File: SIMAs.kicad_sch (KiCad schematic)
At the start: 4 parts, among them U1 mini_esp32, U2 BQ25628ERYKR, U3 TLV61070ADBV, U4 TLV61048DBVR

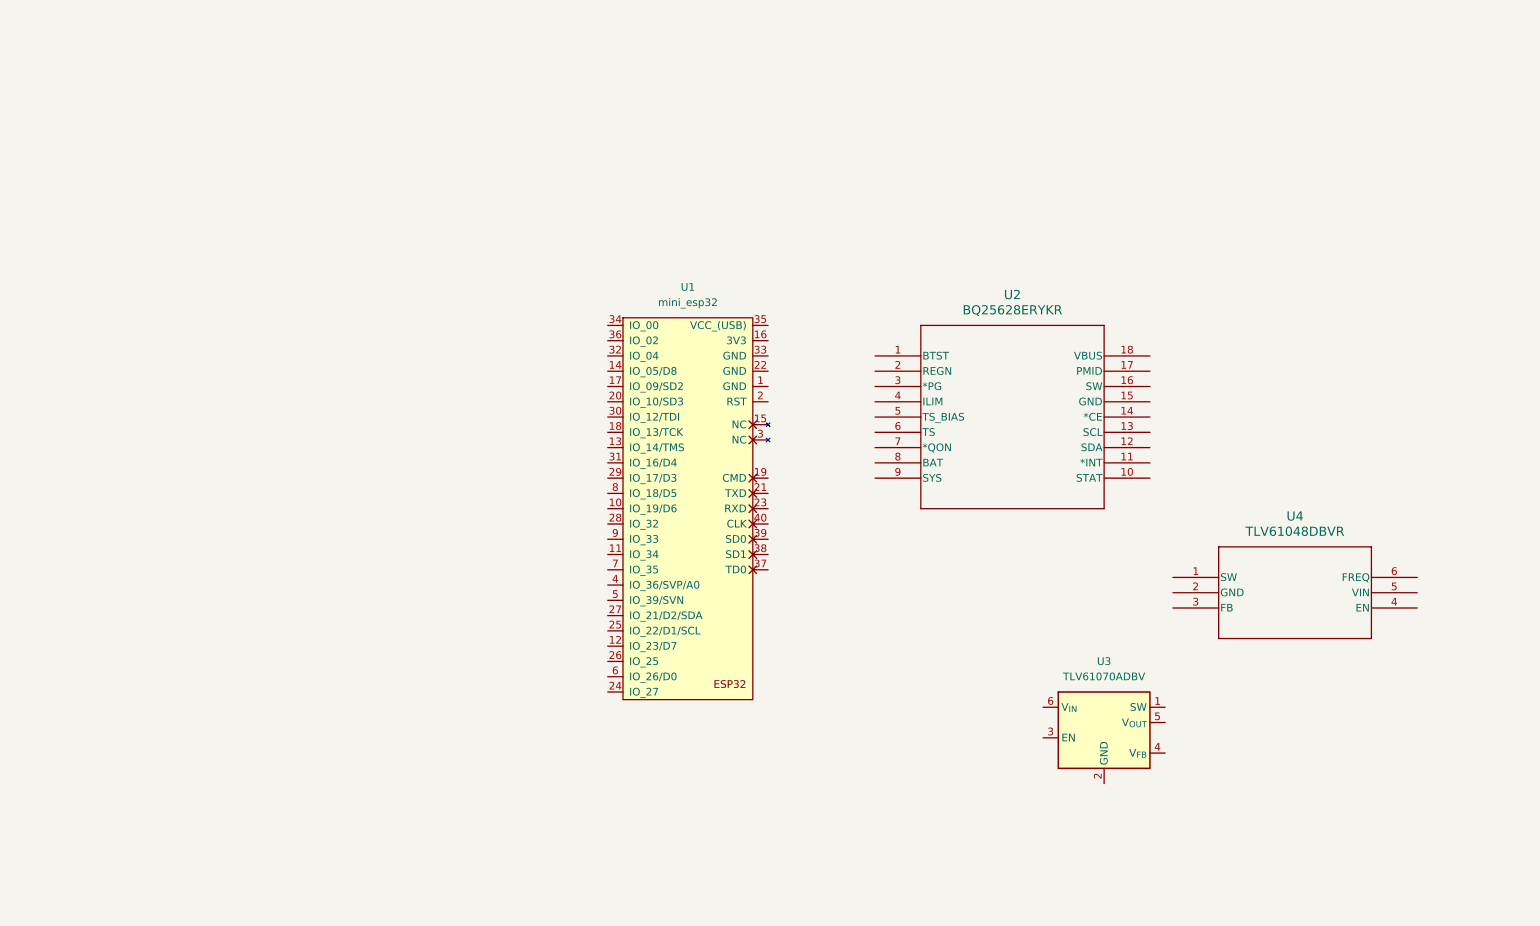
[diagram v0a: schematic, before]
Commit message: Battery charger and 5V boost
Added a herarchical sheet for the poers supply. Done the battery charger and monitor schematic with USB-C charging and the 5 V boost.
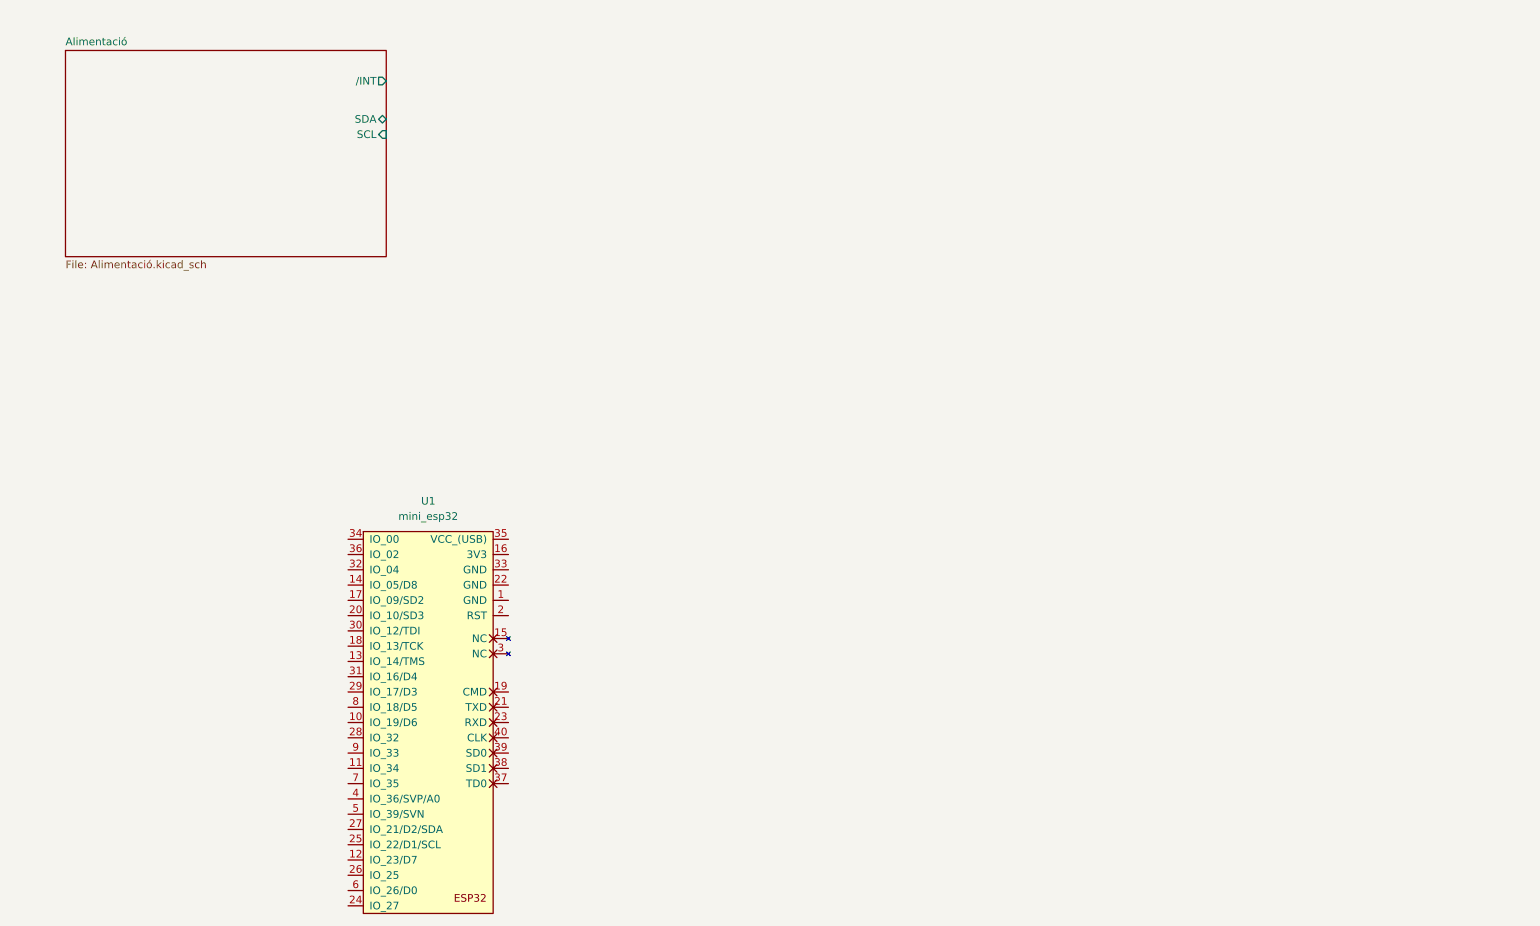
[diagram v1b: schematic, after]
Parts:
- removed U2: BQ25628ERYKR, WQFN-HR18__RYK_TEX, symbol BQ25628E:BQ25628ERYKR
- removed U3: TLV61070ADBV, Package_TO_SOT_SMD:SOT-23-6, symbol Regulator_Switching:TLV61070ADBV
- removed U4: TLV61048DBVR, SOT-23-6_DBV_TEX, symbol TLV61048:TLV61048DBVR
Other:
- added sheet Alimentació (Alimentació.kicad_sch)
- moved on the sheet: U1

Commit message: Canvi
Algu ha canviat, no recordo
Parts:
- added R10, R12, R8: 110, symbol Device:R
- added R11, R13, R9: 2,2 k, symbol Device:R
- added U5, U6, U7: CNY70, OptoDevice:Vishay_CNY70, symbol Sensor_Proximity:CNY70
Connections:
- new net: R10.1, U6.1 (A)
- new net: R12.1, U7.1 (A)
- new net: R8.1, U5.1 (A)
- new net +3.3V: R10.2, R11.2, R12.2, R13.2, R8.2, R9.2
- new net GND: U5.2 (K), U5.4 (E), U6.2 (K), U6.4 (E), U7.2 (K), U7.4 (E)
- new net SENSE_LLUM_1: R9.1, U5.3 (C)
- new net SENSE_LLUM_2: R11.1, R13.1, U6.3 (C), U7.3 (C)
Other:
- added sheet Motors (Motors.kicad_sch)

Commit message: actualitzar ultrima versio pcb/esquematic
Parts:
- added J3, J4, J5: Conn_01x04_Socket, Connector_JST:JST_PH_B4B-PH-K_1x04_P2.00mm_Vertical, symbol Connector:Conn_01x04_Socket
- added J6: Conn_01x03_Socket, Connector_JST:JST_PH_B3B-PH-K_1x03_P2.00mm_Vertical, symbol Connector:Conn_01x03_Socket
- added R28, R29, R30: 110, Resistor_SMD:R_0201_0603Metric, symbol Device:R
- R10, R11, R12, R13, R8, R9: footprint (none) -> Resistor_SMD:R_0201_0603Metric
- U1: footprint (none) -> ESP32_mini:ESP32_mini
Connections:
- net +3.3V: now also J3.1 (Pin_1), J4.1 (Pin_1)
- net Alimentació/SCL: now also U1.25 (IO_22/D1/SCL), R30.1
- net Alimentació/SDA: now also U1.27 (IO_21/D2/SDA), R29.1
- net Alimentació//INT: now also U1.29 (IO_17/D3), R28.1
- net GND: now also U1.22 (GND), J3.4 (Pin_4), J4.4 (Pin_4), J5.4 (Pin_4), J6.3 (Pin_3)
- net ENC3: now reaches U1.11 (IO_34)
- net ENC3: now also J4.2 (Pin_2)
- net nFAULT2: now reaches U1.13 (IO_14/TMS)
- net nFAULT1: now reaches U1.14 (IO_05/D8)
- net at U1.16 (3V3): now also R28.2, R29.2, R30.2
- net IPROPI1: now reaches U1.17 (IO_09/SD2)
- net nSLEEP2: now reaches U1.18 (IO_13/TCK)
- net EN/IN3: now reaches U1.20 (IO_10/SD3)
- net SERVO: now reaches U1.24 (IO_27)
- net SERVO: now also J6.2 (Pin_2)
- net SONS1: now reaches U1.26 (IO_25)
- net SONS1: now also J5.2 (Pin_2)
- net ENC1: now reaches U1.28 (IO_32)
- net ENC1: now also J3.2 (Pin_2)
- net PH/IN4: now reaches U1.30 (IO_12/TDI)
- net IPROPI2: now reaches U1.31 (IO_16/D4)
- net nSLEEP1: now reaches U1.32 (IO_04)
- net EN/IN1: now reaches U1.34 (IO_00)
- net +5V: now reaches U1.35 (VCC_(USB))
- net +5V: now also J5.1 (Pin_1), J6.1 (Pin_1)
- net PH/IN2: now reaches U1.36 (IO_02)
- net SONS2: now reaches U1.6 (IO_26/D0)
- net SONS2: now also J5.3 (Pin_3)
- net ENC4: now reaches U1.7 (IO_35)
- net ENC4: now also J4.3 (Pin_3)
- net ENC2: now reaches U1.9 (IO_33)
- net ENC2: now also J3.3 (Pin_3)
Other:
- moved on the sheet: U1

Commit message: esquematic fet v1
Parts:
- R10, R11, R12, R13, R28, R29, R30, R8, R9: footprint Resistor_SMD:R_0201_0603Metric -> Resistor_SMD:R_0603_1608Metric
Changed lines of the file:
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@@
 			)
 		)
-		(property "Footprint" "Resistor_SMD:R_0201_0603Metric"
+		(property "Footprint" "Resistor_SMD:R_0603_1608Metric"
 			(at 25.908 128.27 90)
 			(effects
@@
 			)
 		)
-		(property "Footprint" "Resistor_SMD:R_0201_0603Metric"
+		(property "Footprint" "Resistor_SMD:R_0603_1608Metric"
 			(at 257.048 33.02 90)
 			(effects
@@
 			)
 		)
-		(property "Footprint" "Resistor_SMD:R_0201_0603Metric"
+		(property "Footprint" "Resistor_SMD:R_0603_1608Metric"
 			(at 185.928 33.02 90)
 			(effects
@@
 			)
 		)
-		(property "Footprint" "Resistor_SMD:R_0201_0603Metric"
+		(property "Footprint" "Resistor_SMD:R_0603_1608Metric"
 			(at 208.788 33.02 90)
 			(effects
@@
 			)
 		)
-		(property "Footprint" "Resistor_SMD:R_0201_0603Metric"
+		(property "Footprint" "Resistor_SMD:R_0603_1608Metric"
 			(at 34.798 128.27 90)
 			(effects
@@
 			)
 		)
-		(property "Footprint" "Resistor_SMD:R_0201_0603Metric"
+		(property "Footprint" "Resistor_SMD:R_0603_1608Metric"
 			(at 43.688 128.27 90)
 			(effects
@@
 			)
 		)
-		(property "Footprint" "Resistor_SMD:R_0201_0603Metric"
+		(property "Footprint" "Resistor_SMD:R_0603_1608Metric"
 			(at 160.528 33.02 90)
 			(effects
@@
 			)
 		)
-		(property "Footprint" "Resistor_SMD:R_0201_0603Metric"
+		(property "Footprint" "Resistor_SMD:R_0603_1608Metric"
 			(at 137.668 33.02 90)
 			(effects
@@
 			)
 		)
-		(property "Footprint" "Resistor_SMD:R_0201_0603Metric"
+		(property "Footprint" "Resistor_SMD:R_0603_1608Metric"
 			(at 234.188 33.02 90)
 			(effects

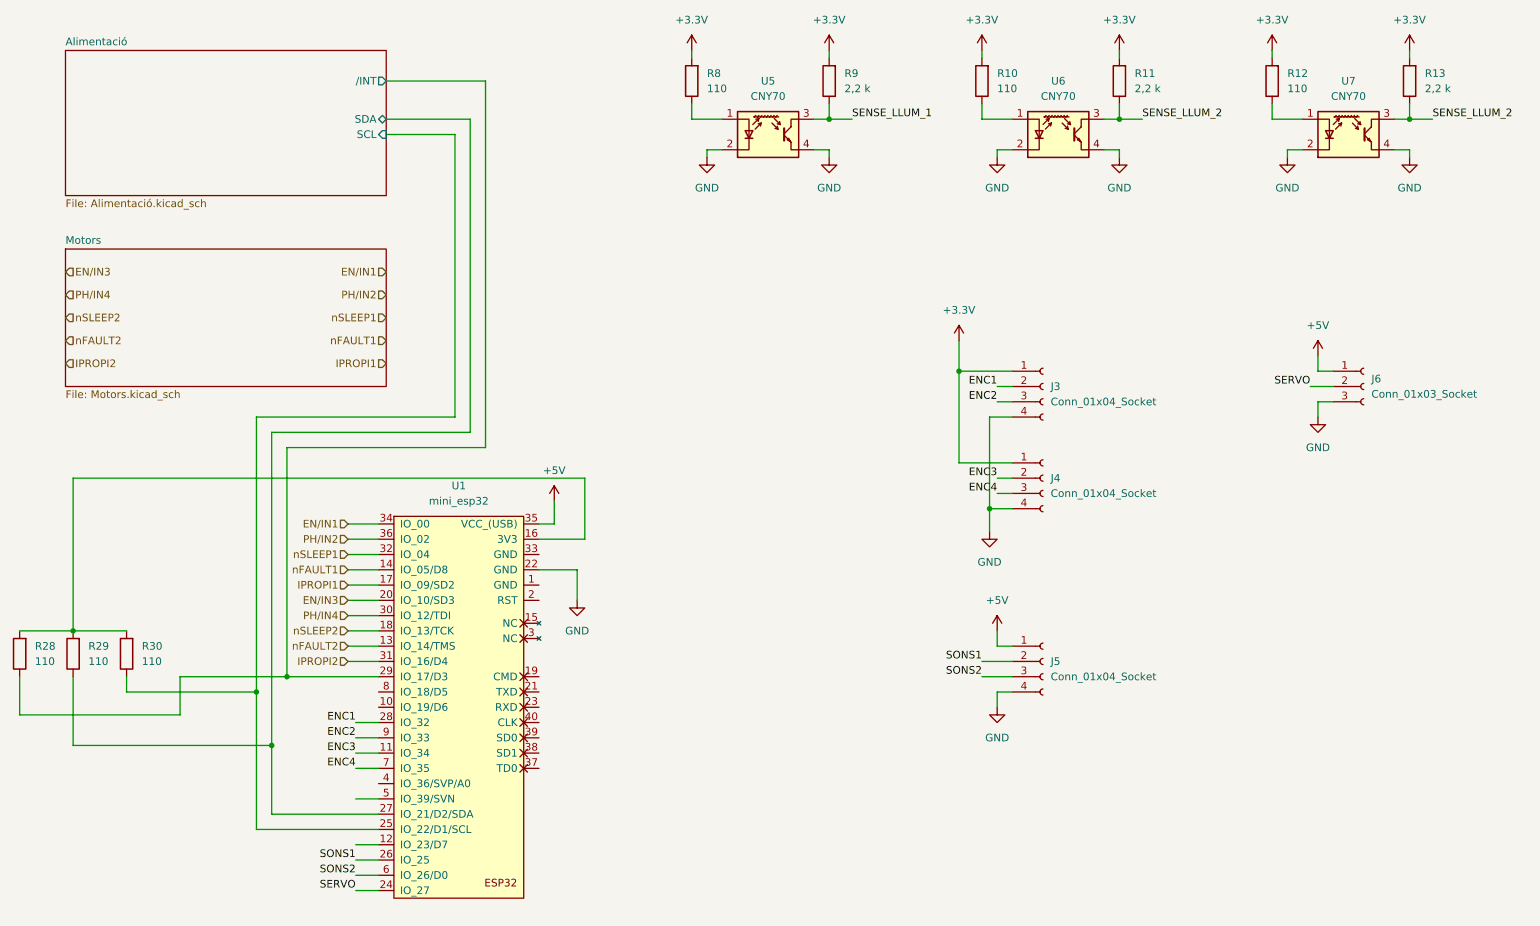
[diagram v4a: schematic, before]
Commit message: Col·locats tots els components
S'han col·locat tots els components a la seva posició a la placa a més d'haver-ne afegit algun més.
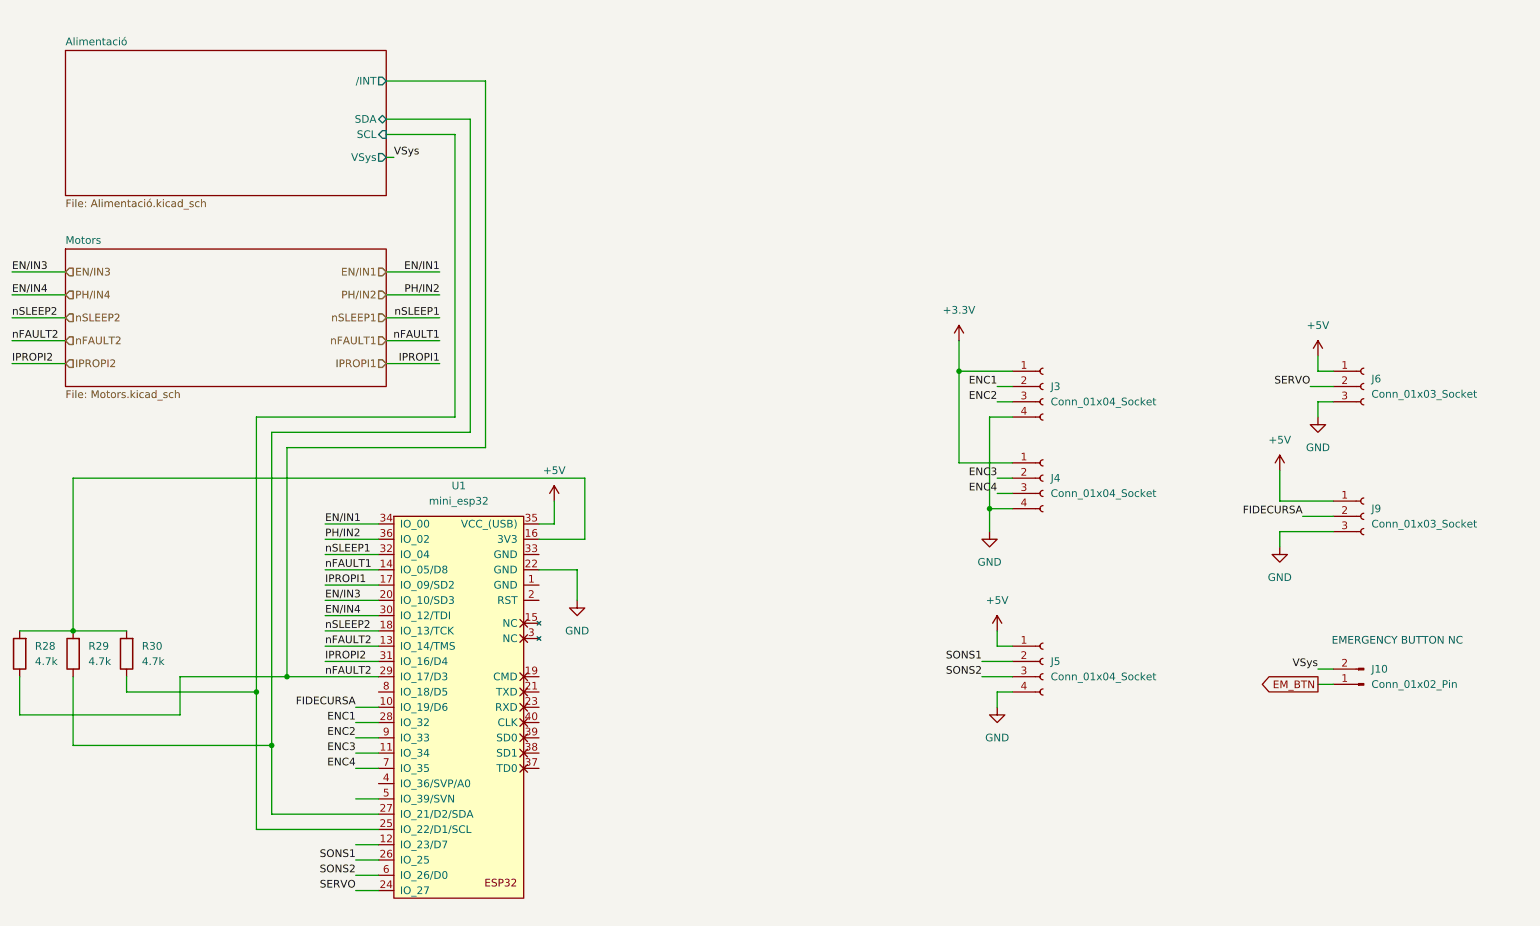
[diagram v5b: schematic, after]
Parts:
- removed R10, R12, R8: 110, Resistor_SMD:R_0603_1608Metric, symbol Device:R
- removed R11, R13, R9: 2,2 k, Resistor_SMD:R_0603_1608Metric, symbol Device:R
- removed U5, U6, U7: CNY70, OptoDevice:Vishay_CNY70, symbol Sensor_Proximity:CNY70
- added J10: Conn_01x02_Pin, Connector_JST:JST_PH_B2B-PH-K_1x02_P2.00mm_Vertical, symbol Connector:Conn_01x02_Pin
- added J9: Conn_01x03_Socket, Connector_JST:JST_PH_B3B-PH-K_1x03_P2.00mm_Vertical, symbol Connector:Conn_01x03_Socket
- R28, R29, R30: value 110 -> 4.7k
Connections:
- net Alimentació//INT is gone; now on net nFAULT2: R28.1, U1.29 (IO_17/D3)
- net +5V: now also J9.1 (Pin_1)
- net GND: now also J9.3 (Pin_3)
- net FIDECURSA: now reaches U1.10 (IO_19/D6)
- net FIDECURSA: now also J9.2 (Pin_2)
- new net EM_BTN: J10.1 (Pin_1)
- new net VSys: J10.2 (Pin_2)
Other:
- sheet Alimentació ports: added VSys; removed none
- note added: "EMERGENCY BUTTON NC"
